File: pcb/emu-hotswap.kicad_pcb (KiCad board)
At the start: 2 copper layers, 157.8 x 118.3 mm, 76 parts, among them J1 TRRS, SW1 SW_Push, SW10 SW_Push, SW11 SW_Push, SW12 SW_Push, SW13 SW_Push, SW14 SW_Push, SW15 SW_Push, SW16 SW_Push, SW17 SW_Push, SW18 SW_Push, SW19 SW_Push, SW2 SW_Push, SW20 SW_Push, SW21 SW_Push, SW22 SW_Push, SW23 SW_Push, SW24 SW_Push, SW25 SW_Push, SW26 SW_Push, SW27 SW_Push, SW28 SW_Push, SW29 SW_Push, SW3 SW_Push, SW30 SW_Push, SW31 SW_Push, SW32 SW_Push, SW4 SW_Push, SW5 SW_Push, SW6 SW_Push, SW7 SW_Push, SW8 SW_Push, SW9 SW_Push, U1 ProMicro

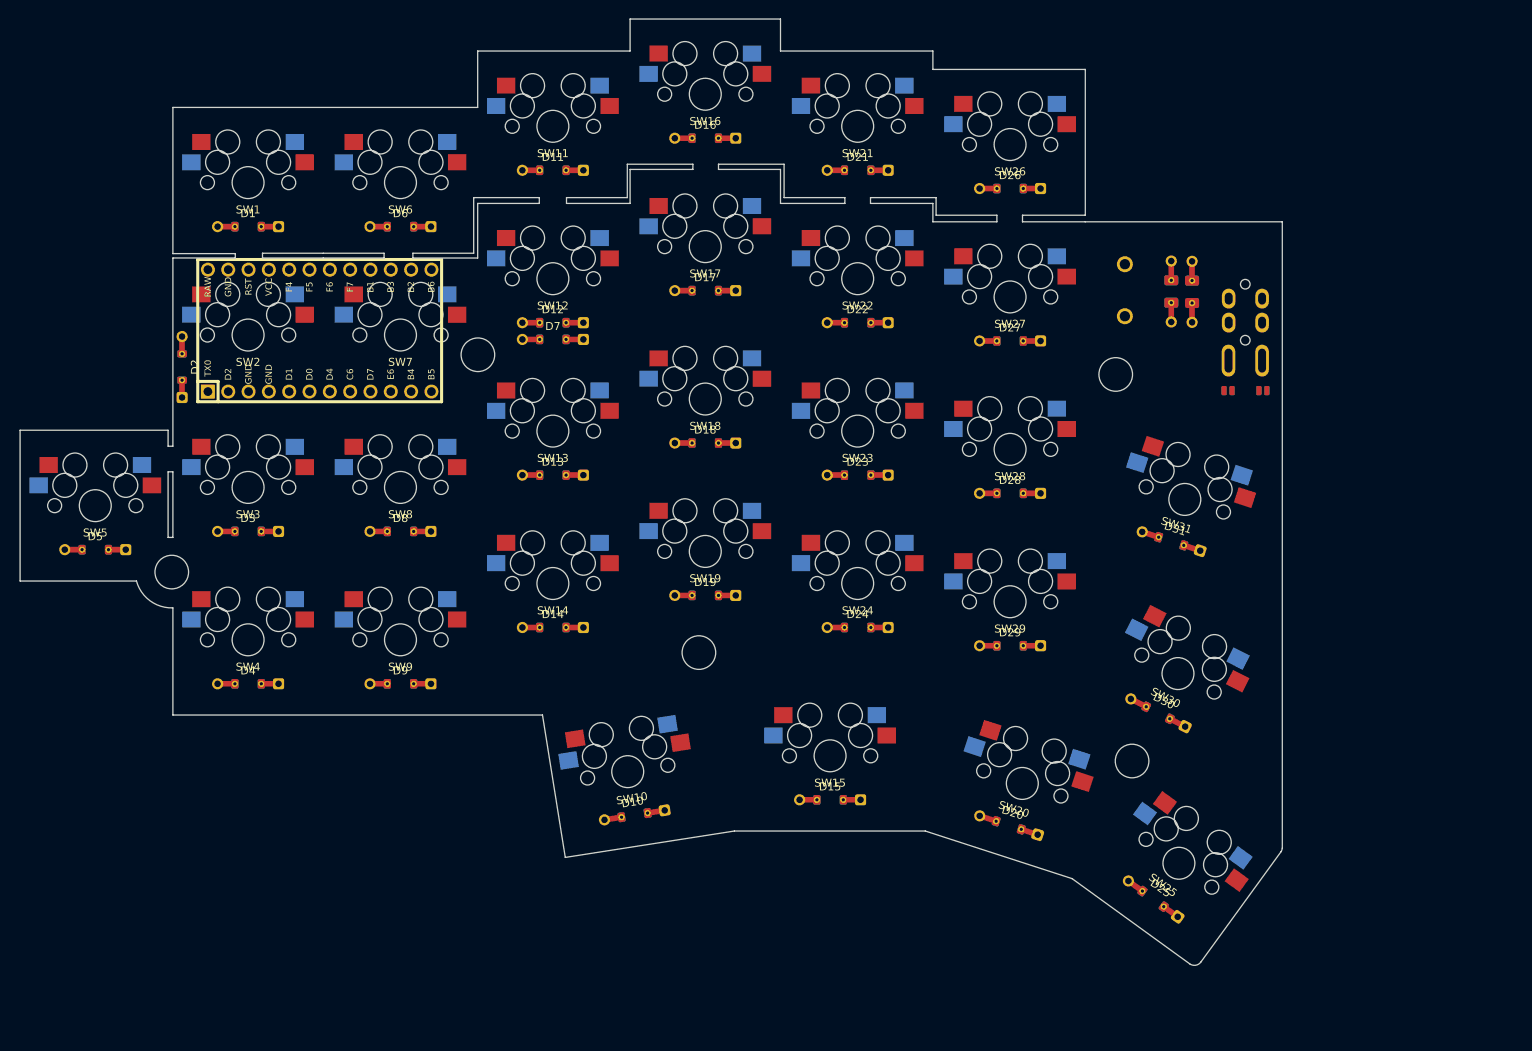
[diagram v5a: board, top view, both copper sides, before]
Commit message: Rounded some edges.
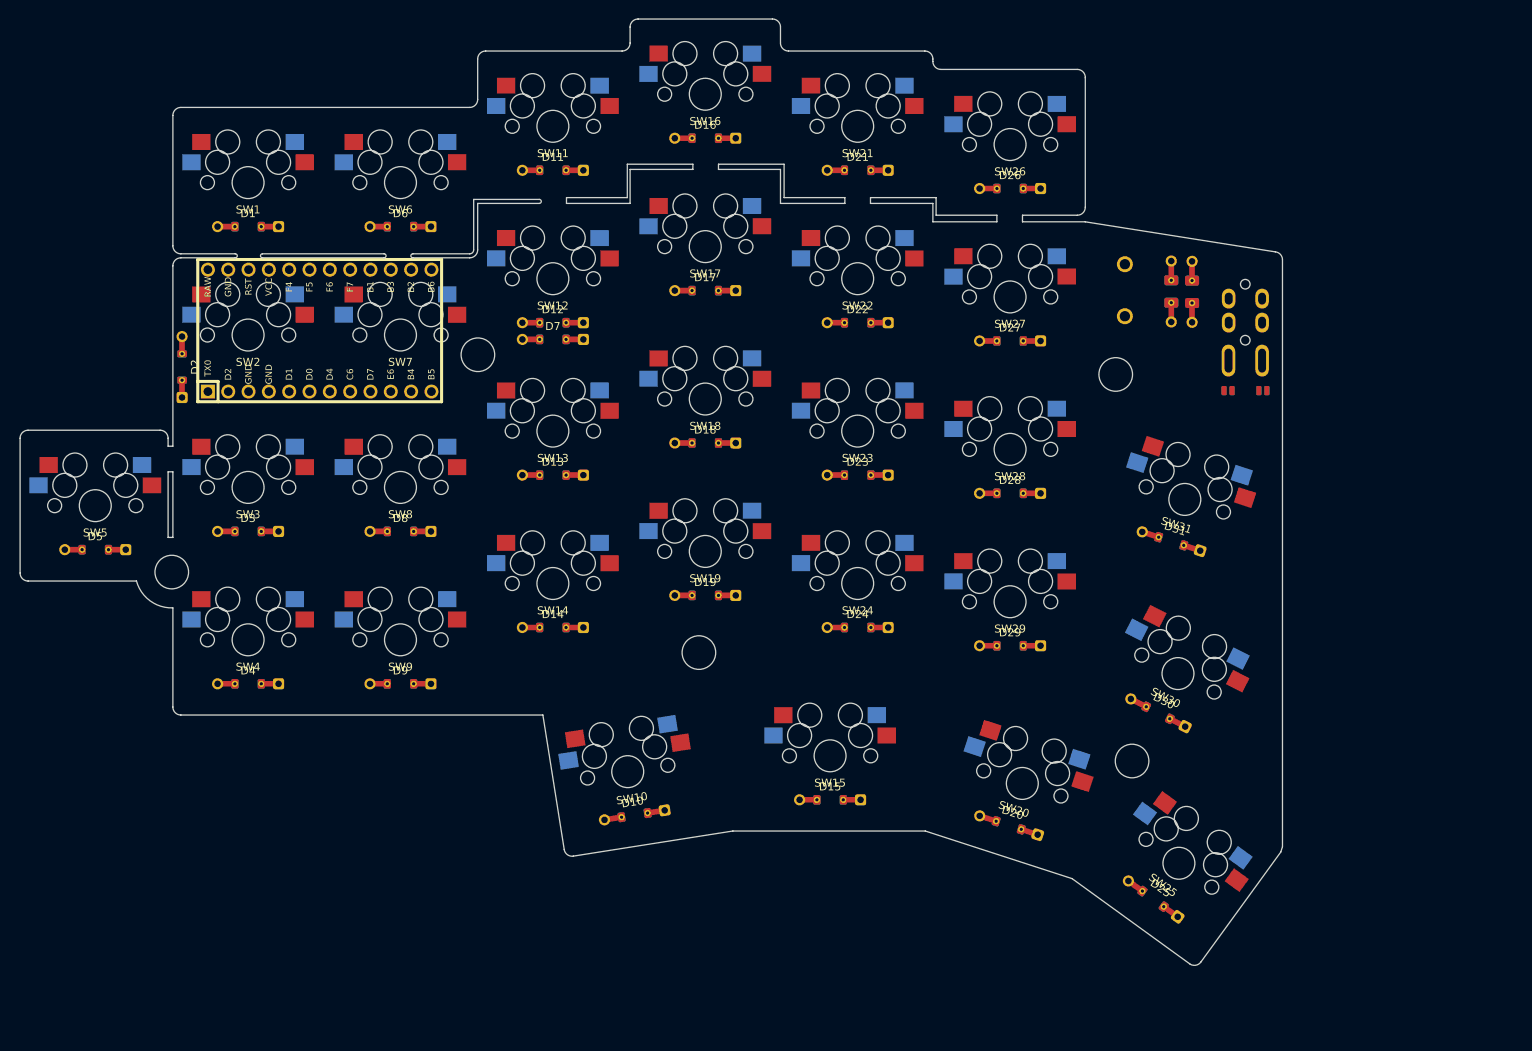
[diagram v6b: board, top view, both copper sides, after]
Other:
- outline, holes or cut-outs redrawn
